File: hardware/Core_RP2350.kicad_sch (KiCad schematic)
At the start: 76 parts, among them J19 Micro_SD_Card_Det_Hirose_DM3AT, J20 USB_C_Receptacle_USB2.0, J21 5-146281-3, J22 5-146281-3, J4 AudioJack3, SW1 SPST-NO, SW2 SPST-NO, SW3 SPST-NO, U1 RP2350B-QFN80, U2 ADUM4160, U3 W25Q128JVS

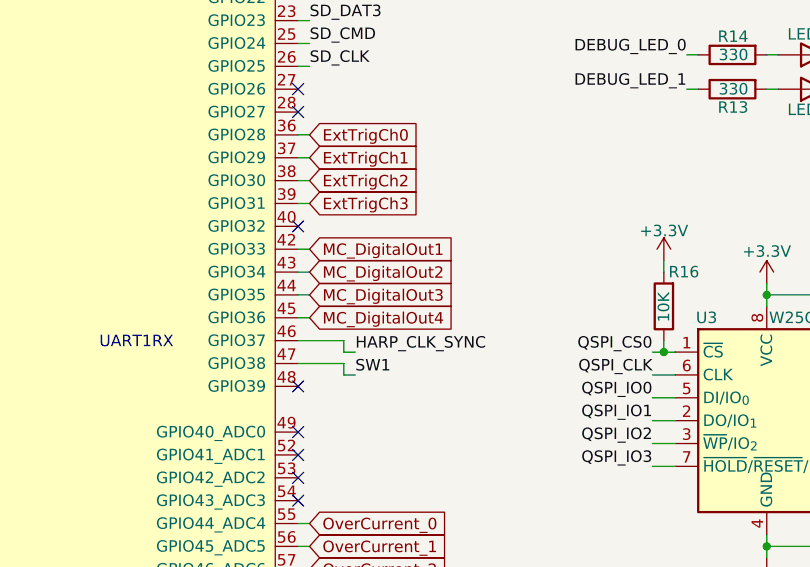
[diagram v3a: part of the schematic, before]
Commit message: cleanup power supply chain
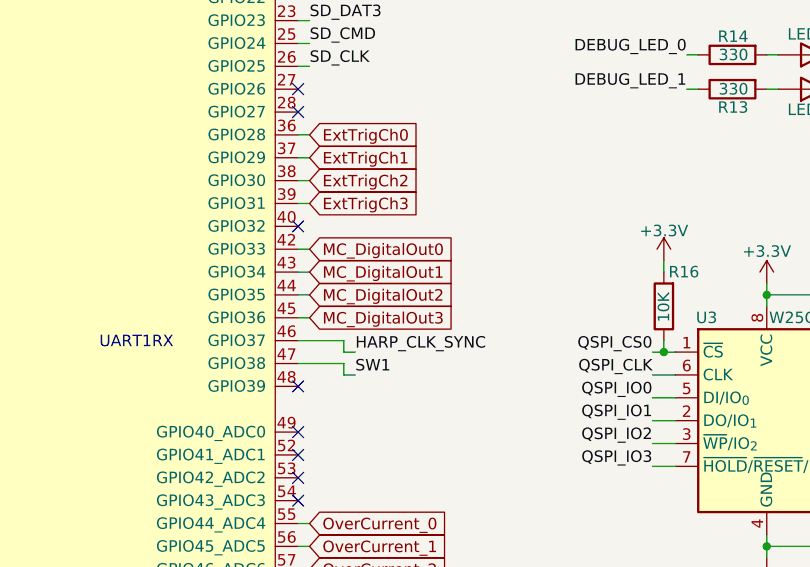
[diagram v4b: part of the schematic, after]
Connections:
- net MC_DigitalOut4 is gone; now on net MC_DigitalOut3: U1.45 (GPIO36)
- net MC_DigitalOut1: now also U1.43 (GPIO34); no longer U1.42 (GPIO33)
- net MC_DigitalOut2: now also U1.44 (GPIO35); no longer U1.43 (GPIO34)
- net MC_DigitalOut3: no longer U1.44 (GPIO35)
- new net MC_DigitalOut0: U1.42 (GPIO33)
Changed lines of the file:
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@@
 		)
 	)
-	(global_label "MC_DigitalOut4"
+	(global_label "MC_DigitalOut3"
 		(shape input)
 		(at 138.43 133.35 0)
@@
 		)
 	)
+	(global_label "MC_DigitalOut1"
+		(shape input)
+		(at 138.43 128.27 0)
+		(fields_autoplaced yes)
+		(effects
+			(font
+				(size 1.27 1.27)
+			)
+			(justify left)
+		)
+		(property "Intersheetrefs" "${INTERSHEET_REFS}"
+			(at 155.6874 128.27 0)
+			(effects
+				(font
+					(size 1.27 1.27)
+				)
+				(justify left)
+				(hide yes)
+			)
+		)
+	)
+	(global_label "DAC_0_DIN"
+		(shape input)
+		(at 138.43 52.07 0)
+		(fields_autoplaced yes)
+		(effects
+			(font
+				(size 1.27 1.27)
+			)
+			(justify left)
+		)
+		(property "Intersheetrefs" "${INTERSHEET_REFS}"
+			(at 151.3938 52.07 0)
+			(effects
+				(font
+					(size 1.27 1.27)
+				)
+				(justify left)
+				(hide yes)
+			)
+		)
+	)
+	(global_label "DAC_2_SCK"
+		(shape input)
+		(at 138.43 74.93 0)
+		(fields_autoplaced yes)
+		(effects
+			(font
+				(size 1.27 1.27)
+			)
+			(justify left)
+		)
+		(property "Intersheetrefs" "${INTERSHEET_REFS}"
+			(at 151.938 74.93 0)
+			(effects
+				(font
+					(size 1.27 1.27)
+				)
+				(justify left)
+				(hide yes)
+			)
+		)
+	)
+	(global_label "ExtTrigCh1"
+		(shape input)
+		(at 138.43 115.57 0)
+		(fields_autoplaced yes)
+		(effects
+			(font
+				(size 1.27 1.27)
+			)
+			(justify left)
+		)
+		(property "Intersheetrefs" "${INTERSHEET_REFS}"
+			(at 151.4541 115.57 0)
+			(effects
+				(font
+					(size 1.27 1.27)
+				)
+				(justify left)
+				(hide yes)
+			)
+		)
+	)
+	(global_label "DAC_1_CS"
+		(shape input)
+		(at 138.43 67.31 0)
+		(fields_autoplaced yes)
+		(effects
+			(font
+				(size 1.27 1.27)
+			)
+			(justify left)
+		)
+		(property "Intersheetrefs" "${INTERSHEET_REFS}"
+			(at 150.668 67.31 0)
+			(effects
+				(font
+					(size 1.27 1.27)
+				)
+				(justify left)
+				(hide yes)
+			)
+		)
+	)
+	(global_label "SHORT_CIRCUIT_2"
+		(shape input)
+		(at 138.43 80.01 0)
+		(fields_autoplaced yes)
+		(effects
+			(font
+				(size 1.27 1.27)
+			)
+			(justify left)
+		)
+		(property "Intersheetrefs" "${INTERSHEET_REFS}"
+			(at 157.9857 80.01 0)
+			(effects
+				(font
+					(size 1.27 1.27)
+				)
+				(justify left)
+				(hide yes)
+			)
+		)
+	)
+	(global_label "DAC_3_SCK"
+		(shape input)
+		(at 138.43 85.09 0)
+		(fields_autoplaced yes)
+		(effects
+			(font
+				(size 1.27 1.27)
+			)
+			(justify left)
+		)
+		(property "Intersheetrefs" "${INTERSHEET_REFS}"
+			(at 151.938 85.09 0)
+			(effects
+				(font
+					(size 1.27 1.27)
+				)
+				(justify left)
+				(hide yes)
+			)
+		)
+	)
+	(global_label "SHORT_CIRCUIT_1"
+		(shape input)
+		(at 138.43 69.85 0)
+		(fields_autoplaced yes)
+		(effects
+			(font
+				(size 1.27 1.27)
+			)
+			(justify left)
+		)
+		(property "Intersheetrefs" "${INTERSHEET_REFS}"
+			(at 157.9857 69.85 0)
+			(effects
+				(font
+					(size 1.27 1.27)
+				)
+				(justify left)
+				(hide yes)
+			)
+		)
+	)
+	(global_label "DAC_0_SCK"
+		(shape input)
+		(at 138.43 54.61 0)
+		(fields_autoplaced yes)
+		(effects
+			(font
+				(size 1.27 1.27)
+			)
+			(justify left)
+		)
+		(property "Intersheetrefs" "${INTERSHEET_REFS}"
+			(at 151.938 54.61 0)
+			(effects
+				(font
+					(size 1.27 1.27)
+				)
+				(justify left)
+				(hide yes)
+			)
+		)
+	)
+	(global_label "DAC_3_DIN"
+		(shape input)
+		(at 138.43 82.55 0)
+		(fields_autoplaced yes)
+		(effects
+			(font
+				(size 1.27 1.27)
+			)
+			(justify left)
+		)
+		(property "Intersheetrefs" "${INTERSHEET_REFS}"
+			(at 151.3938 82.55 0)
+			(effects
+				(font
+					(size 1.27 1.27)
+				)
+				(justify left)
+				(hide yes)
+			)
+		)
+	)
 	(global_label "MC_DigitalOut2"
 		(shape input)
-		(at 138.43 128.27 0)
-		(fields_autoplaced yes)
-		(effects
-			(font
-				(size 1.27 1.27)
-			)
-			(justify left)
-		)
-		(property "Intersheetrefs" "${INTERSHEET_REFS}"
-			(at 155.6874 128.27 0)
-			(effects
-				(font
-					(size 1.27 1.27)
-				)
-				(justify left)
-				(hide yes)
-			)
-		)
-	)
-	(global_label "DAC_0_DIN"
-		(shape input)
-		(at 138.43 52.07 0)
-		(fields_autoplaced yes)
-		(effects
-			(font
-				(size 1.27 1.27)
-			)
-			(justify left)
-		)
-		(property "Intersheetrefs" "${INTERSHEET_REFS}"
-			(at 151.3938 52.07 0)
-			(effects
-				(font
-					(size 1.27 1.27)
-				)
-				(justify left)
-				(hide yes)
-			)
-		)
-	)
-	(global_label "DAC_2_SCK"
-		(shape input)
-		(at 138.43 74.93 0)
-		(fields_autoplaced yes)
-		(effects
-			(font
-				(size 1.27 1.27)
-			)
-			(justify left)
-		)
-		(property "Intersheetrefs" "${INTERSHEET_REFS}"
-			(at 151.938 74.93 0)
-			(effects
-				(font
-					(size 1.27 1.27)
-				)
-				(justify left)
-				(hide yes)
-			)
-		)
-	)
-	(global_label "ExtTrigCh1"
-		(shape input)
-		(at 138.43 115.57 0)
-		(fields_autoplaced yes)
-		(effects
-			(font
-				(size 1.27 1.27)
-			)
-			(justify left)
-		)
-		(property "Intersheetrefs" "${INTERSHEET_REFS}"
-			(at 151.4541 115.57 0)
-			(effects
-				(font
-					(size 1.27 1.27)
-				)
-				(justify left)
-				(hide yes)
-			)
-		)
-	)
-	(global_label "DAC_1_CS"
-		(shape input)
-		(at 138.43 67.31 0)
-		(fields_autoplaced yes)
-		(effects
-			(font
-				(size 1.27 1.27)
-			)
-			(justify left)
-		)
-		(property "Intersheetrefs" "${INTERSHEET_REFS}"
-			(at 150.668 67.31 0)
-			(effects
-				(font
-					(size 1.27 1.27)
-				)
-				(justify left)
-				(hide yes)
-			)
-		)
-	)
-	(global_label "SHORT_CIRCUIT_2"
-		(shape input)
-		(at 138.43 80.01 0)
-		(fields_autoplaced yes)
-		(effects
-			(font
-				(size 1.27 1.27)
-			)
-			(justify left)
-		)
-		(property "Intersheetrefs" "${INTERSHEET_REFS}"
-			(at 157.9857 80.01 0)
-			(effects
-				(font
-					(size 1.27 1.27)
-				)
-				(justify left)
-				(hide yes)
-			)
-		)
-	)
-	(global_label "DAC_3_SCK"
-		(shape input)
-		(at 138.43 85.09 0)
-		(fields_autoplaced yes)
-		(effects
-			(font
-				(size 1.27 1.27)
-			)
-			(justify left)
-		)
-		(property "Intersheetrefs" "${INTERSHEET_REFS}"
-			(at 151.938 85.09 0)
-			(effects
-				(font
-					(size 1.27 1.27)
-				)
-				(justify left)
-				(hide yes)
-			)
-		)
-	)
-	(global_label "SHORT_CIRCUIT_1"
-		(shape input)
-		(at 138.43 69.85 0)
-		(fields_autoplaced yes)
-		(effects
-			(font
-				(size 1.27 1.27)
-			)
-			(justify left)
-		)
-		(property "Intersheetrefs" "${INTERSHEET_REFS}"
-			(at 157.9857 69.85 0)
-			(effects
-				(font
-					(size 1.27 1.27)
-				)
-				(justify left)
-				(hide yes)
-			)
-		)
-	)
-	(global_label "DAC_0_SCK"
-		(shape input)
-		(at 138.43 54.61 0)
-		(fields_autoplaced yes)
-		(effects
-			(font
-				(size 1.27 1.27)
-			)
-			(justify left)
-		)
-		(property "Intersheetrefs" "${INTERSHEET_REFS}"
-			(at 151.938 54.61 0)
-			(effects
-				(font
-					(size 1.27 1.27)
-				)
-				(justify left)
-				(hide yes)
-			)
-		)
-	)
-	(global_label "DAC_3_DIN"
-		(shape input)
-		(at 138.43 82.55 0)
-		(fields_autoplaced yes)
-		(effects
-			(font
-				(size 1.27 1.27)
-			)
-			(justify left)
-		)
-		(property "Intersheetrefs" "${INTERSHEET_REFS}"
-			(at 151.3938 82.55 0)
-			(effects
-				(font
-					(size 1.27 1.27)
-				)
-				(justify left)
-				(hide yes)
-			)
-		)
-	)
-	(global_label "MC_DigitalOut3"
-		(shape input)
 		(at 138.43 130.81 0)
 		(fields_autoplaced yes)
@@
 		)
 	)
-	(global_label "MC_DigitalOut1"
+	(global_label "MC_DigitalOut0"
 		(shape input)
 		(at 138.43 125.73 0)

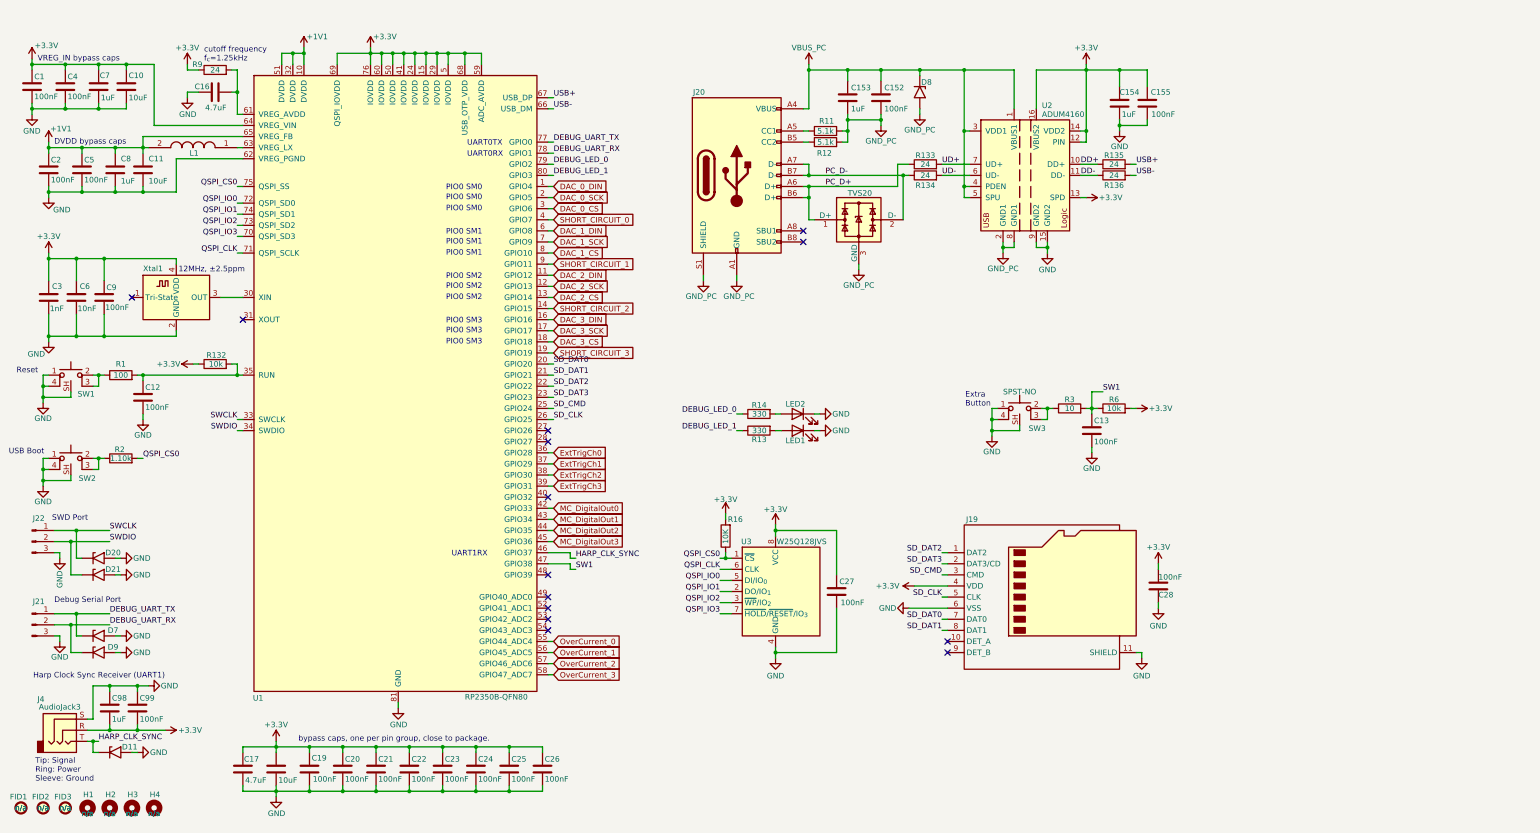
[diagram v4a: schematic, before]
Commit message: update tvs diodes, regulators, and power supply chain
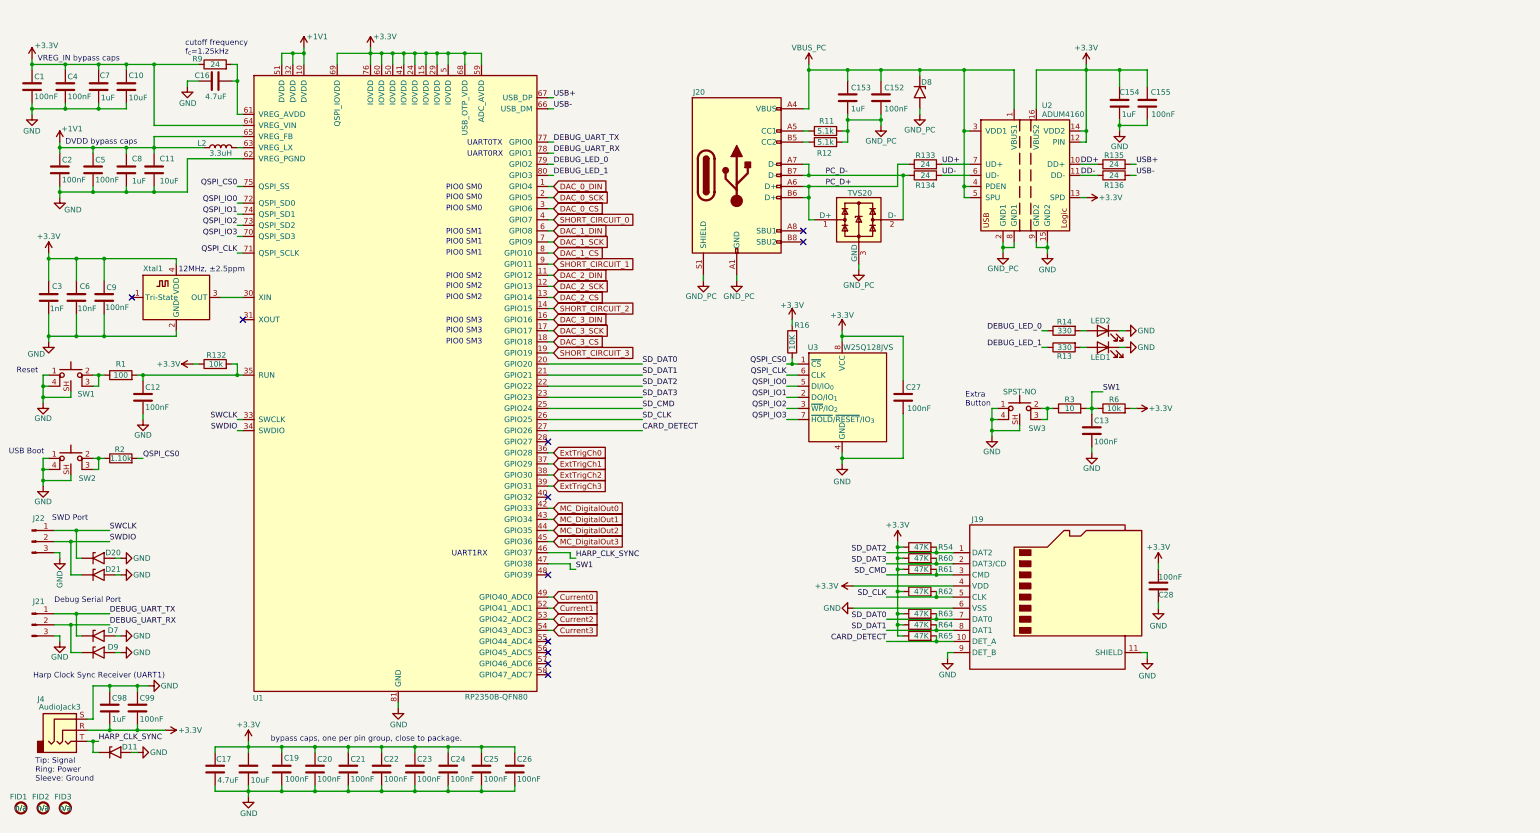
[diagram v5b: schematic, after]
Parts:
- removed H1, H2, H3, H4: MountingHole_Pad, harp.device.quad.dac.kicad:MountingHole_3.2mm_M3_DIN965, symbol harp.device.quad.dac:MountingHole_Pad
- removed L1: XGL3530-332MEC, harp.device.quad.dac.kicad:XGL3530332MEC, symbol harp.device.quad.dac:XGL3530-332MEC
- added L2: 3.3uH, kicad_component_library:L_0806_2016Metric, symbol Device:L
- added R54, R60, R61, R62, R63, R64, R65: 47K, symbol Device:R
- C1, C12, C13, C152, C155, C19, C2, C20, C21, C22, C23, C24, C25, C26, C27, C28, C4, C5, C9, C99: Manufacturer Number (none) -> C0603C104K5RACTU
- C10, C11, C18: Manufacturer Number (none) -> GRM188R61E106KA73D
- C153, C154, C7, C8, C98: Manufacturer Number (none) -> C1608X7R1H105K080AB
- C16, C17: Manufacturer Number (none) -> C1608X5R1V475K080AC
- C3: Manufacturer Number (none) -> C0603C102K5RACTU
- C6: Manufacturer Number (none) -> C0603C103K5RACTU
- J19: Link (none) -> https://www.digikey.com/en/products/detail/hirose-electric-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; Manufacturer (none) -> Hirose Electric Co Ltd; Manufacturer Number (none) -> DM3AT-SF-PEJM5
- LED1, LED2: Link https://www.digikey.com/en/products/detail/sunled/XZCDGK53W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 -> (none); Manufacturer_Name Vishay -> (none); Manufacturer_Part_Number VLMS1300-GS08 -> (none)
- U1: Manufacturer Number (none) -> SC1510-A4
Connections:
- net +1V1: now also L2.1
- net +3.3V: now also R54.1, R60.1, R61.1, R62.1, R63.1, R64.1, R65.1
- net GND: now also J19.9 (DET_B)
- net SD_CLK: now also R62.2
- net SD_CMD: now also R61.2
- net SD_DAT0: now also R63.2
- net SD_DAT1: now also R64.2
- net SD_DAT2: now also R54.2
- net SD_DAT3: now also R60.2
- net at U1.63 (VREG_LX): now also L2.2
- net CARD_DETECT: now reaches U1.27 (GPIO26)
- net CARD_DETECT: now also J19.10 (DET_A), R65.2
- net Current0: now reaches U1.49 (GPIO40_ADC0)
- net Current1: now reaches U1.52 (GPIO41_ADC1)
- net Current2: now reaches U1.53 (GPIO42_ADC2)
- net Current3: now reaches U1.54 (GPIO43_ADC3)
- net OverCurrent_0: no longer names the net of U1.55 (GPIO44_ADC4)
- net OverCurrent_1: no longer names the net of U1.56 (GPIO45_ADC5)
- net OverCurrent_2: no longer names the net of U1.57 (GPIO46_ADC6)
- net OverCurrent_3: no longer names the net of U1.58 (GPIO47_ADC7)
- no-connect marks 14 -> 11
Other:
- title: harp device quad dac -> harp.device.quad-dac
- moved on the sheet: C11, C16, C17, C19, C2, C20, C21, C22, C23, C24, C25, C26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
